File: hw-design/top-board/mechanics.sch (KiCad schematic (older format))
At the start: 11 parts

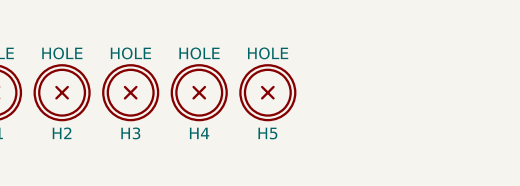
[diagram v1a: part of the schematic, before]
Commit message: added new components and footprints
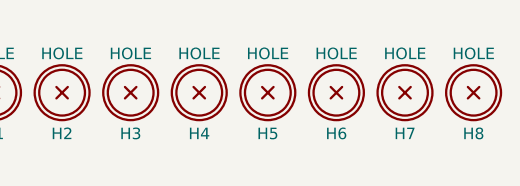
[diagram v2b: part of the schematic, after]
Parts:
- added H6, H7, H8: HOLE, footprints:Hole_3.5mm, symbol HOLE
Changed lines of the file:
@@
 EESchema Schematic File Version 2
-LIBS:top-board-rescue
 LIBS:power
-LIBS:device
-LIBS:conn
-LIBS:regul
-LIBS:74xgxx
 LIBS:local-components
+LIBS:Video
+LIBS:Valve
+LIBS:Triac_Thyristor
+LIBS:Transistor_IGBT
+LIBS:Transistor_FET
+LIBS:Transistor_BJT
+LIBS:Transistor_Array
+LIBS:Transformer
+LIBS:Timer_RTC
+LIBS:Timer_PLL
+LIBS:Timer
+LIBS:Switch
+LIBS:Sensor_Voltage
+LIBS:Sensor_Touch
+LIBS:Sensor_Temperature
+LIBS:Sensor_Proximity
+LIBS:Sensor_Pressure
+LIBS:Sensor_Optical
+LIBS:Sensor_Motion
+LIBS:Sensor_Magnetic
+LIBS:Sensor_Humidity
+LIBS:Sensor_Gas
+LIBS:Sensor_Current
+LIBS:Sensor_Audio
+LIBS:Sensor
+LIBS:RF_ZigBee
+LIBS:RF_WiFi
+LIBS:RF_Switch
+LIBS:RF_RFID
+LIBS:RF_Module
+LIBS:RF_Mixer
+LIBS:RF_GPS
+LIBS:RF_Bluetooth
+LIBS:RF_Amplifier
+LIBS:RF_AM_FM
+LIBS:RF
+LIBS:Relay_SolidState
+LIBS:Relay
+LIBS:Regulator_Switching
+LIBS:Regulator_SwitchedCapacitor
+LIBS:Regulator_Linear
+LIBS:Regulator_Current
+LIBS:Regulator_Controller
+LIBS:Reference_Voltage
+LIBS:Reference_Current
+LIBS:pspice
+LIBS:Power_Supervisor
+LIBS:Power_Protection
+LIBS:Power_Management
+LIBS:Potentiometer_Digital
+LIBS:Oscillator
+LIBS:Motor
+LIBS:Memory_UniqueID
+LIBS:Memory_ROM
+LIBS:Memory_RAM
+LIBS:Memory_NVRAM
+LIBS:Memory_Flash
+LIBS:Memory_EPROM
+LIBS:Memory_EEPROM
+LIBS:Memory_Controller
+LIBS:Mechanical
+LIBS:MCU_Texas_MSP430
+LIBS:MCU_Texas
+LIBS:MCU_ST_STM32L4+
+LIBS:MCU_ST_STM32L4
+LIBS:MCU_ST_STM32L1
+LIBS:MCU_ST_STM32L0
+LIBS:MCU_ST_STM32H7
+LIBS:MCU_ST_STM32F7
+LIBS:MCU_ST_STM32F4
+LIBS:MCU_ST_STM32F3
+LIBS:MCU_ST_STM32F2
+LIBS:MCU_ST_STM32F1
+LIBS:MCU_ST_STM32F0
+LIBS:MCU_ST_STM8
+LIBS:MCU_SiliconLabs
+LIBS:MCU_SiFive
+LIBS:MCU_Parallax
+LIBS:MCU_NXP_S08
+LIBS:MCU_NXP_MCore
+LIBS:MCU_NXP_MAC7100
+LIBS:MCU_NXP_LPC
+LIBS:MCU_NXP_Kinetis
+LIBS:MCU_NXP_HCS12
+LIBS:MCU_NXP_HC12
+LIBS:MCU_NXP_HC11
+LIBS:MCU_NXP_ColdFire
+LIBS:MCU_Nordic
+LIBS:MCU_Module
+LIBS:MCU_Microchip_SAML
+LIBS:MCU_Microchip_SAME
+LIBS:MCU_Microchip_PIC32
+LIBS:MCU_Microchip_PIC24
+LIBS:MCU_Microchip_PIC18
+LIBS:MCU_Microchip_PIC16
+LIBS:MCU_Microchip_PIC12
+LIBS:MCU_Microchip_PIC10
+LIBS:MCU_Microchip_AVR
+LIBS:MCU_Microchip_ATtiny
+LIBS:MCU_Microchip_ATmega
+LIBS:MCU_Microchip_8051
+LIBS:MCU_Intel
+LIBS:MCU_Espressif
+LIBS:MCU_Cypress
+LIBS:MCU_AnalogDevices
+LIBS:Logic_Programmable
+LIBS:Logic_LevelTranslator
+LIBS:LED
+LIBS:Jumper
+LIBS:Isolator_Analog
+LIBS:Isolator
+LIBS:Interface_USB
+LIBS:Interface_UART
+LIBS:Interface_Telecom
+LIBS:Interface_Optical
+LIBS:Interface_LineDriver
+LIBS:Interface_HID
+LIBS:Interface_Expansion
+LIBS:Interface_Ethernet
+LIBS:Interface_CurrentLoop
+LIBS:Interface_CAN_LIN
+LIBS:Interface
+LIBS:Graphic
+LIBS:GPU
+LIBS:FPGA_Xilinx_Virtex7
+LIBS:FPGA_Xilinx_Virtex6
+LIBS:FPGA_Xilinx_Virtex5
+LIBS:FPGA_Xilinx_Spartan6
+LIBS:FPGA_Xilinx_Kintex7
+LIBS:FPGA_Xilinx_Artix7
+LIBS:FPGA_Xilinx
+LIBS:FPGA_Microsemi
+LIBS:Filter
+LIBS:DSP_Texas
+LIBS:DSP_Motorola
+LIBS:DSP_Microchip_DSPIC33
+LIBS:DSP_Freescale
+LIBS:Driver_Relay
+LIBS:Driver_Motor
+LIBS:Driver_LED
+LIBS:Driver_FET
+LIBS:Driver_Display
+LIBS:Display_Graphic
+LIBS:Display_Character
+LIBS:Diode_Laser
+LIBS:Diode_Bridge
+LIBS:Diode
+LIBS:Device
+LIBS:CPU_PowerPC
+LIBS:CPU_NXP_68000
+LIBS:CPU_NXP_6800
+LIBS:CPU
+LIBS:CPLD_Xilinx
+LIBS:CPLD_Altera
+LIBS:Converter_DCDC
+LIBS:Converter_ACDC
+LIBS:Connector_Generic_Shielded
+LIBS:Connector_Generic_MountingPin
+LIBS:Connector_Generic
+LIBS:Connector
+LIBS:Comparator
+LIBS:Battery_Management
+LIBS:Audio
+LIBS:Analog_Switch
+LIBS:Analog_DAC
+LIBS:Analog_ADC
+LIBS:Analog
+LIBS:Amplifier_Video
+LIBS:Amplifier_Operational
+LIBS:Amplifier_Instrumentation
+LIBS:Amplifier_Difference
+LIBS:Amplifier_Current
+LIBS:Amplifier_Buffer
+LIBS:Amplifier_Audio
+LIBS:74xx_IEEE
+LIBS:74xx
+LIBS:74xGxx
+LIBS:4xxx_IEEE
+LIBS:4xxx
+LIBS:button_wLED
 LIBS:top-board-cache
 EELAYER 25 0
@@
 	1    0    0    -1
 $EndComp
+$Comp
+L HOLE H6
+U 1 1 5AF07001
+P 6400 1150
+F 0 "H6" H 6400 970 50  0000 C CNN
+F 1 "HOLE" H 6400 1320 50  0000 C CNN
+F 2 "footprints:Hole_3.5mm" H 6400 1150 60  0001 C CNN
+F 3 "" H 6400 1150 60  0000 C CNN
+	1    6400 1150
+	1    0    0    -1
+$EndComp
+$Comp
+L HOLE H7
+U 1 1 5AF0703D
+P 6700 1150
+F 0 "H7" H 6700 970 50  0000 C CNN
+F 1 "HOLE" H 6700 1320 50  0000 C CNN
+F 2 "footprints:Hole_3.5mm" H 6700 1150 60  0001 C CNN
+F 3 "" H 6700 1150 60  0000 C CNN
+	1    6700 1150
+	1    0    0    -1
+$EndComp
+$Comp
+L HOLE H8
+U 1 1 5AF07092
+P 7000 1150
+F 0 "H8" H 7000 970 50  0000 C CNN
+F 1 "HOLE" H 7000 1320 50  0000 C CNN
+F 2 "footprints:Hole_3.5mm" H 7000 1150 60  0001 C CNN
+F 3 "" H 7000 1150 60  0000 C CNN
+	1    7000 1150
+	1    0    0    -1
+$EndComp
